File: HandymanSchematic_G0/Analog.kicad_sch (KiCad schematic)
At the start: 57 parts, among them Q1 BC847, Q2 BC847, U1 TL074, U201 TL074, U202 TL072

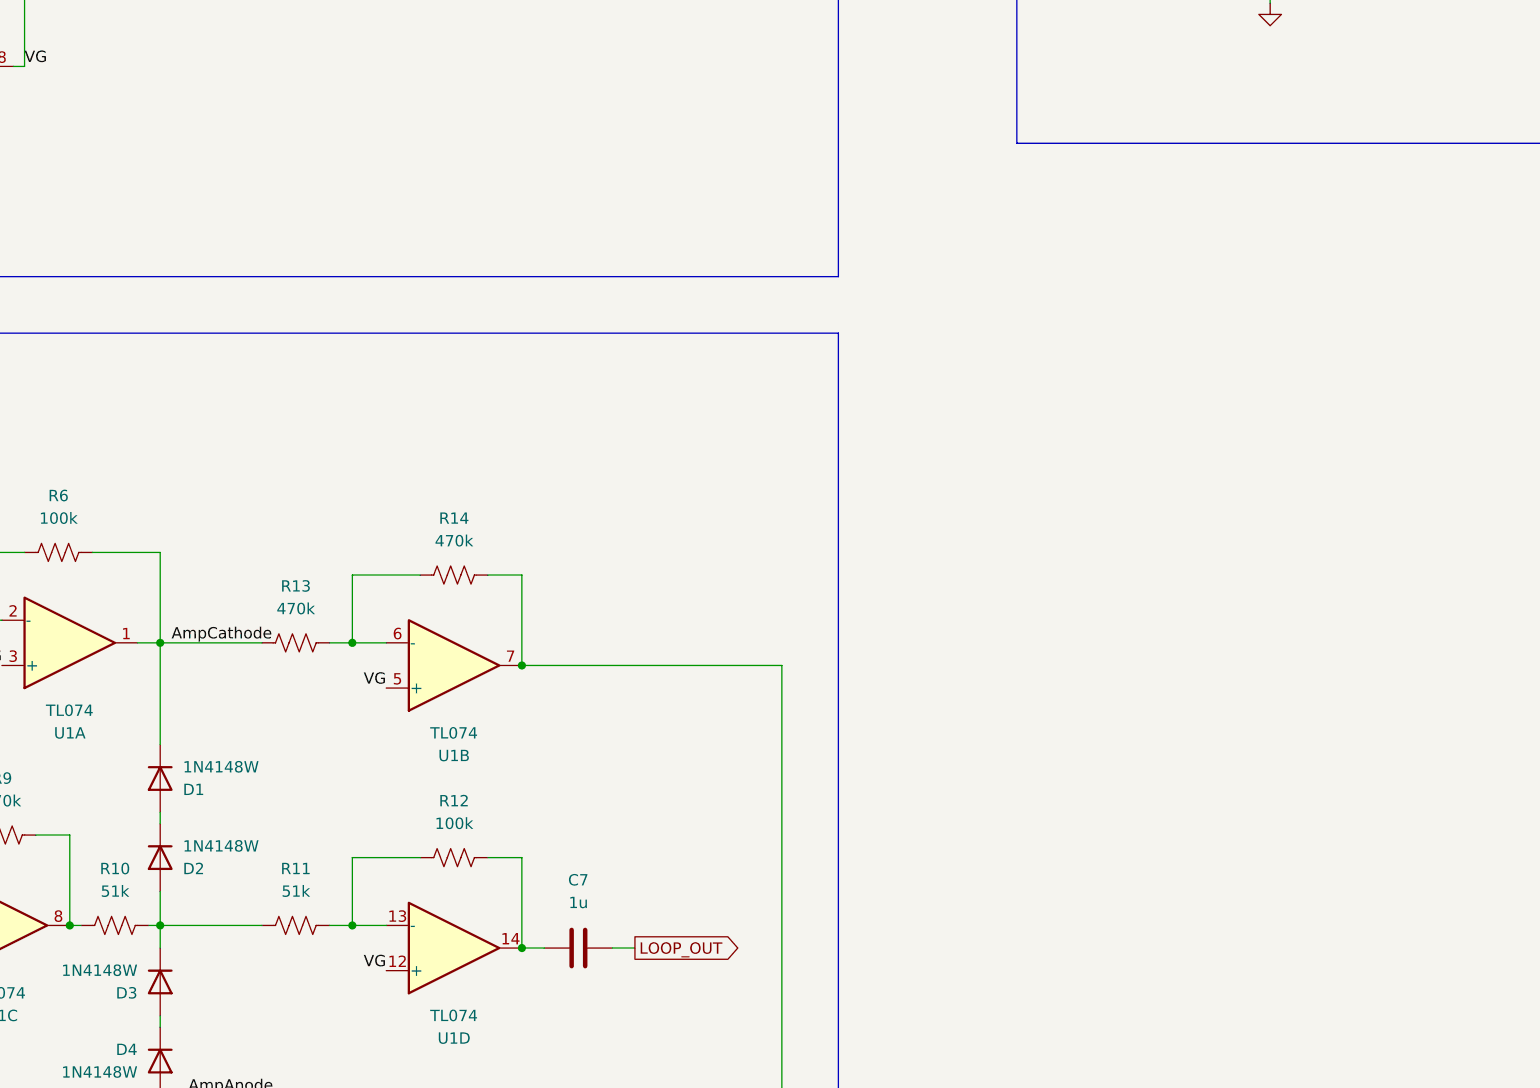
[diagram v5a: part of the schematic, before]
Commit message: footprints chosen, test points
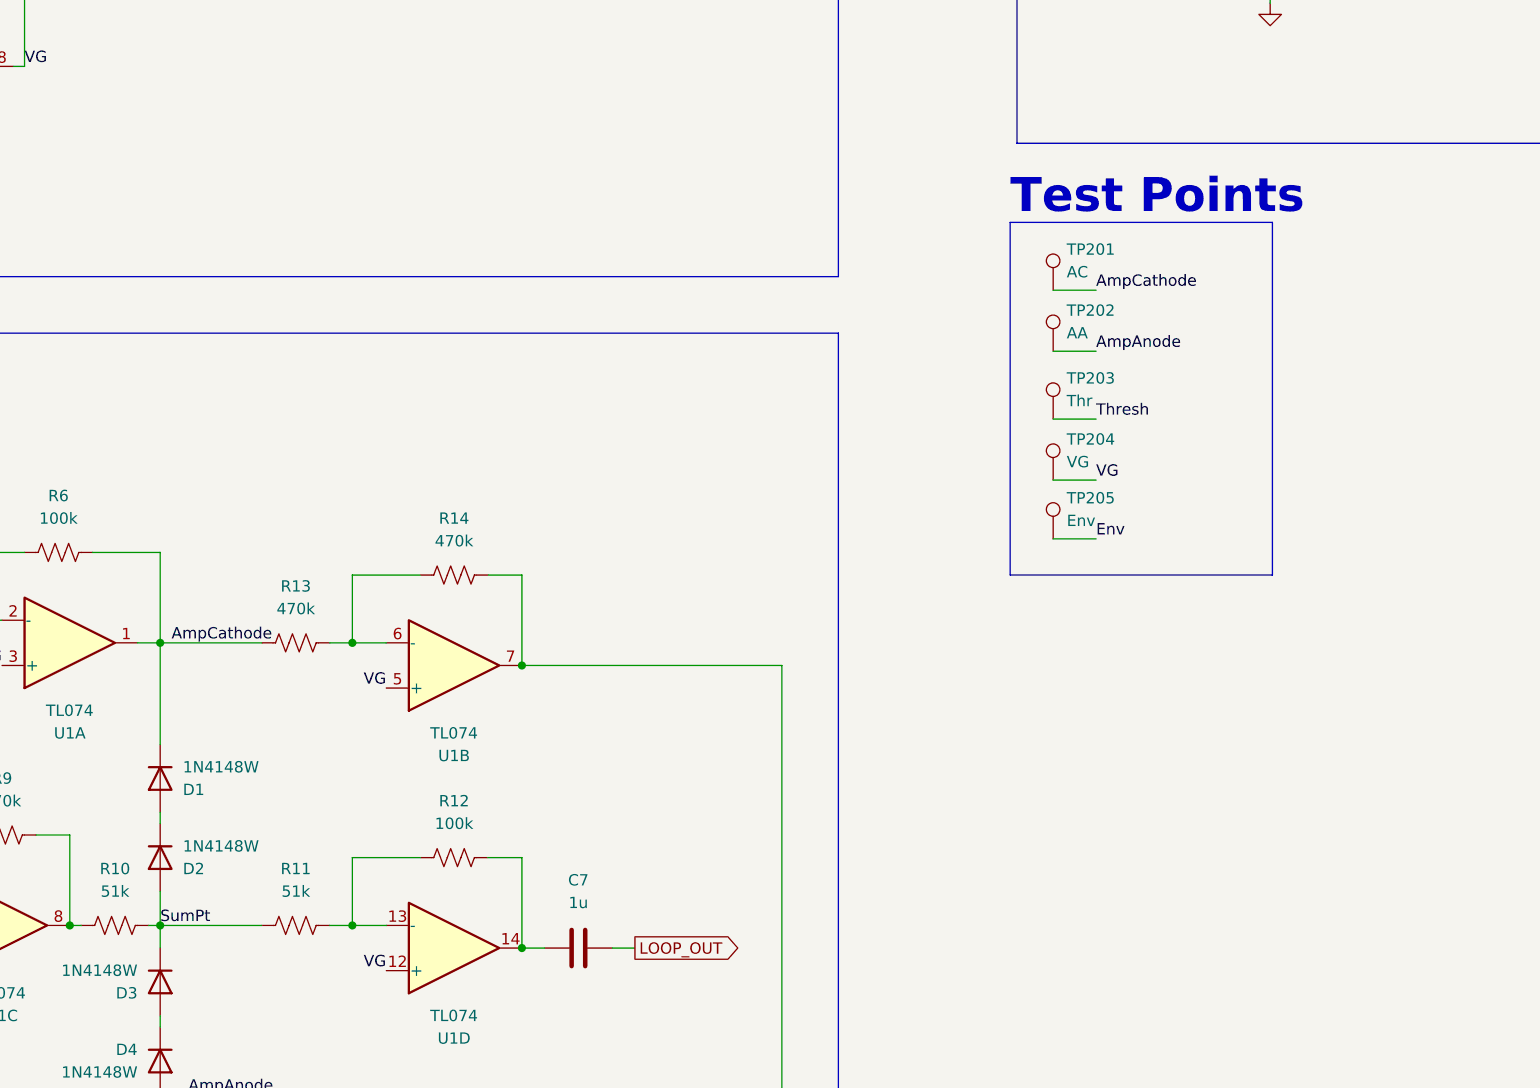
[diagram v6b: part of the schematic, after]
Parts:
- added TP201: AC, TestPoint:TestPoint_THTPad_D2.0mm_Drill1.0mm_VAL, symbol Connector:TestPoint
- added TP202: AA, TestPoint:TestPoint_THTPad_D2.0mm_Drill1.0mm_VAL, symbol Connector:TestPoint
- added TP203: Thr, TestPoint:TestPoint_THTPad_D2.0mm_Drill1.0mm_VAL, symbol Connector:TestPoint
- added TP204: VG, TestPoint:TestPoint_THTPad_D2.0mm_Drill1.0mm_VAL, symbol Connector:TestPoint
- added TP205: Env, TestPoint:TestPoint_THTPad_D2.0mm_Drill1.0mm_VAL, symbol Connector:TestPoint
- C1, C2, C202, C203, C204, C205, C206, C207, C208, C3, C4, C5, C6, C7: footprint (none) -> Capacitor_SMD:C_0805_2012Metric
- R1, R10, R11, R12, R13, R14, R16, R17, R2, R203, R204, R205, R206, R207, R208, R209, R211, R212, R3, R4, R5, R6, R7, R8, R9: footprint (none) -> Resistor_SMD:R_0805_2012Metric
- RV1, RV201: footprint (none) -> Potentiometer_THT:Potentiometer_Alpha_RV16AF_42_Single_Long
- U1: footprint (none) -> Package_SO:SOIC-14_3.9x8.7mm_P1.27mm
- U202: footprint (none) -> Package_SO:SOIC-8_3.9x4.9mm_P1.27mm
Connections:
- net AmpAnode: now also TP202.1
- net AmpCathode: now also TP201.1
- net Env: now also TP205.1
- net Thresh: now also TP203.1
- net VG: now also TP204.1
- net SumPt: now reaches D2.2 (A), D3.1 (K), R10.2, R11.1
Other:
- note added: "Test Points"

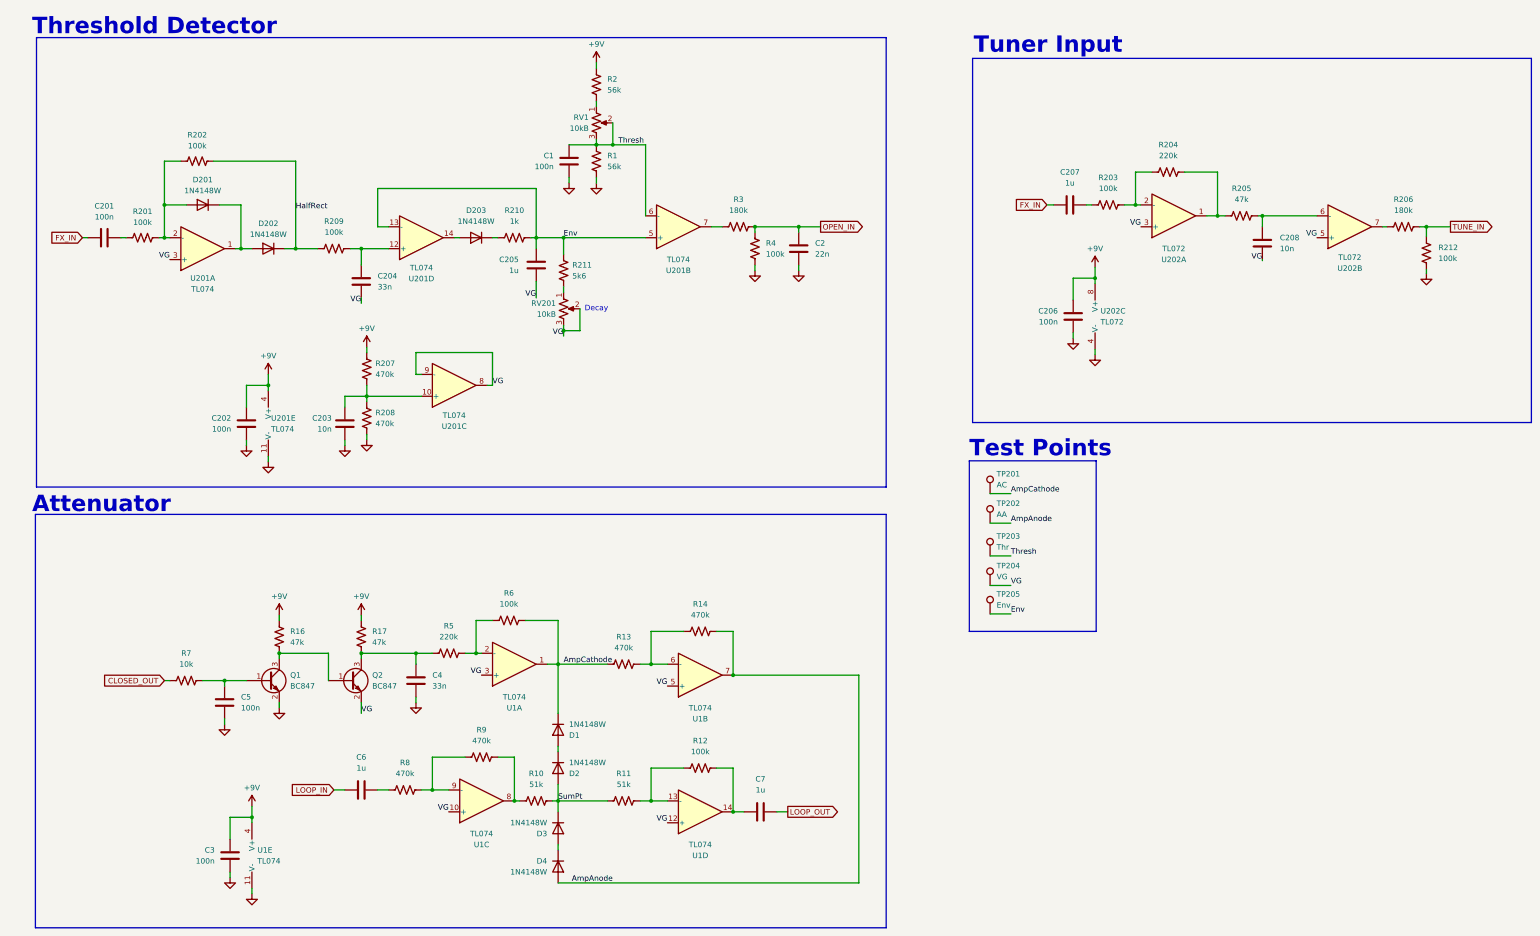
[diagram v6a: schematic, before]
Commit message: footprints, enclosure areas drawn
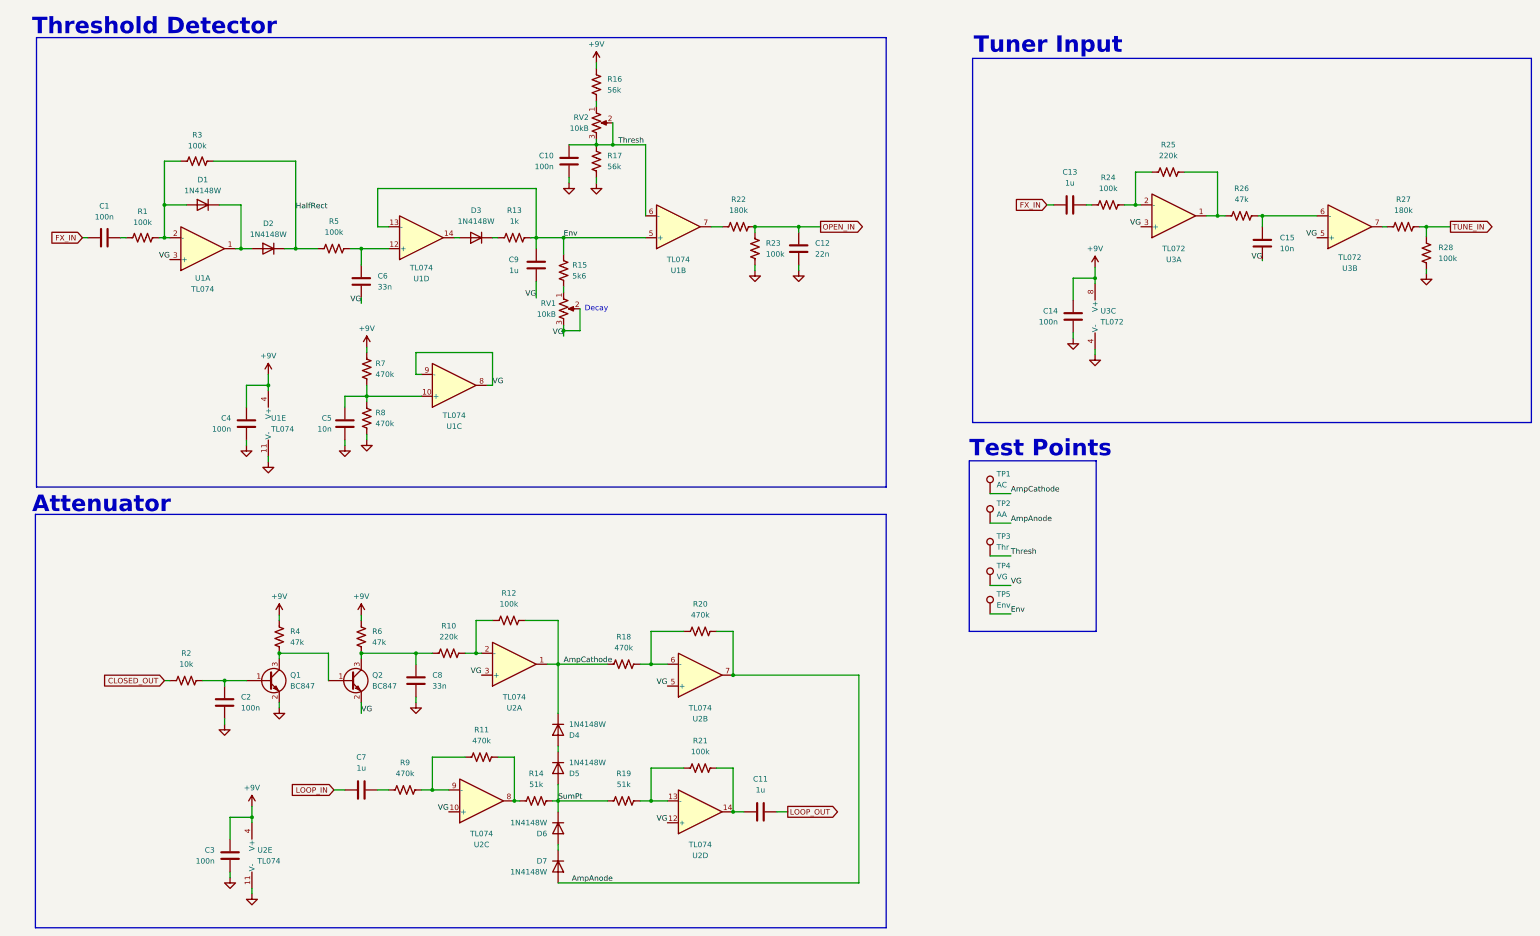
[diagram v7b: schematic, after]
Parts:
- renumbered C201 to C1, C1 to C10, C7 to C11, C2 to C12, C207 to C13, C206 to C14, C208 to C15, C5 to C2, C202 to C4, C203 to C5, C204 to C6, C6 to C7, C4 to C8, C205 to C9, D201 to D1, D202 to D2, D203 to D3, D1 to D4, D2 to D5, D3 to D6, D4 to D7, R201 to R1, R5 to R10, R9 to R11, R6 to R12, R210 to R13, R10 to R14, R211 to R15, R2 to R16, R1 to R17, R13 to R18, R11 to R19, R7 to R2, R14 to R20, R12 to R21, R3 to R22, R4 to R23, R203 to R24, R204 to R25, R205 to R26, R206 to R27, R212 to R28, R202 to R3, R16 to R4, R209 to R5, R17 to R6, R207 to R7, R208 to R8, R8 to R9, RV201 to RV1, RV1 to RV2, TP201 to TP1, TP202 to TP2, TP203 to TP3, TP204 to TP4, TP205 to TP5, U201 to U1, U1 to U2, U202 to U3

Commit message: analog side layout
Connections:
- net Env: now also U1.10 (+); no longer U1.5 (+)
- net Thresh: now also U1.9 (-); no longer U1.6 (-)
- net VG: now also U1.6 (-), U1.7; no longer U1.8, U1.9 (-)
- net at C5.1, R7.2, R8.1: now also U1.5 (+); no longer U1.10 (+)
- net at R22.1: now also U1.8; no longer U1.7
- no-connect marks 0 -> 1
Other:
- moved on the sheet: U1B, U1C
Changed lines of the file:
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@@
 		(color 0 0 0 0)
 	)
+	(no_connect
+		(at 124.46 107.95)
+	)
 	(wire
 		(pts
@@
 	(symbol
 		(lib_id "Amplifier_Operational:TL074")
-		(at 116.84 101.6 0)
+		(at 168.91 64.77 0)
 		(mirror x)
 		(unit 3)
@@
 		(dnp no)
 		(property "Reference" "U1"
-			(at 116.84 111.125 0)
+			(at 168.91 74.295 0)
 			(effects
 				(font
@@
 		)
 		(property "Value" "TL074"
-			(at 116.84 108.585 0)
+			(at 168.91 71.755 0)
 			(effects
 				(font
@@
 		)
 		(property "Footprint" "Package_SO:SOIC-14_3.9x8.7mm_P1.27mm"
-			(at 115.57 104.14 0)
+			(at 167.64 67.31 0)
 			(effects
 				(font
@@
 		)
 		(property "Datasheet" "http://www.ti.com/lit/ds/symlink/tl071.pdf"
-			(at 118.11 106.68 0)
+			(at 170.18 69.85 0)
 			(effects
 				(font
@@
 		)
 		(property "Description" "Quad Low-Noise JFET-Input Operational Amplifiers, DIP-14/SOIC-14"
-			(at 116.84 101.6 0)
+			(at 168.91 64.77 0)
 			(effects
 				(font
@@
 	(symbol
 		(lib_id "Amplifier_Operational:TL074")
-		(at 168.91 64.77 0)
+		(at 116.84 101.6 0)
 		(mirror x)
 		(unit 2)
@@
 		(dnp no)
 		(property "Reference" "U1"
-			(at 168.91 74.93 0)
+			(at 116.84 111.76 0)
 			(effects
 				(font
@@
 		)
 		(property "Value" "TL074"
-			(at 168.91 72.39 0)
+			(at 116.84 109.22 0)
 			(effects
 				(font
@@
 		)
 		(property "Footprint" "Package_SO:SOIC-14_3.9x8.7mm_P1.27mm"
-			(at 167.64 67.31 0)
+			(at 115.57 104.14 0)
 			(effects
 				(font
@@
 		)
 		(property "Datasheet" "http://www.ti.com/lit/ds/symlink/tl071.pdf"
-			(at 170.18 69.85 0)
+			(at 118.11 106.68 0)
 			(effects
 				(font
@@
 		)
 		(property "Description" "Quad Low-Noise JFET-Input Operational Amplifiers, DIP-14/SOIC-14"
-			(at 168.91 64.77 0)
+			(at 116.84 101.6 0)
 			(effects
 				(font
